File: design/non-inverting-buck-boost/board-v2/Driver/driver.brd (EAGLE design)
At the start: 5 parts

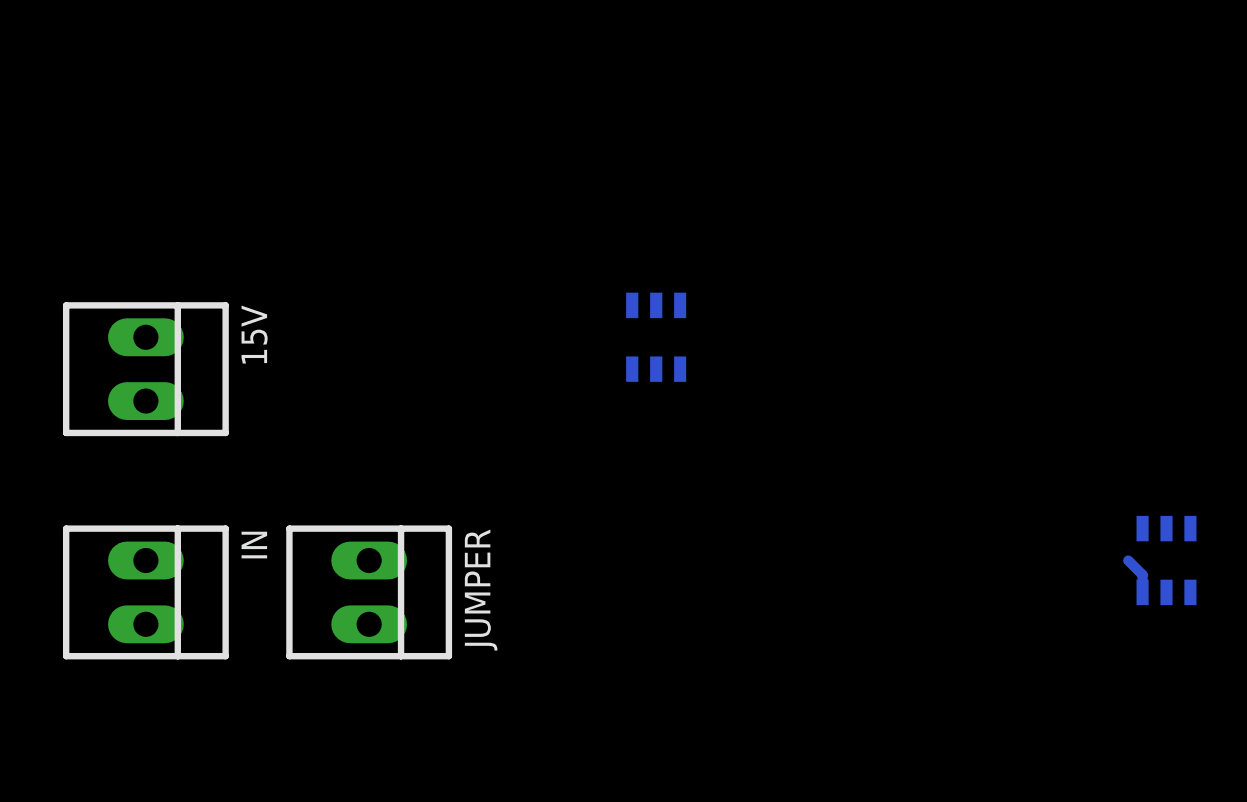
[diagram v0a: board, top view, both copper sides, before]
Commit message: finished driver board layout
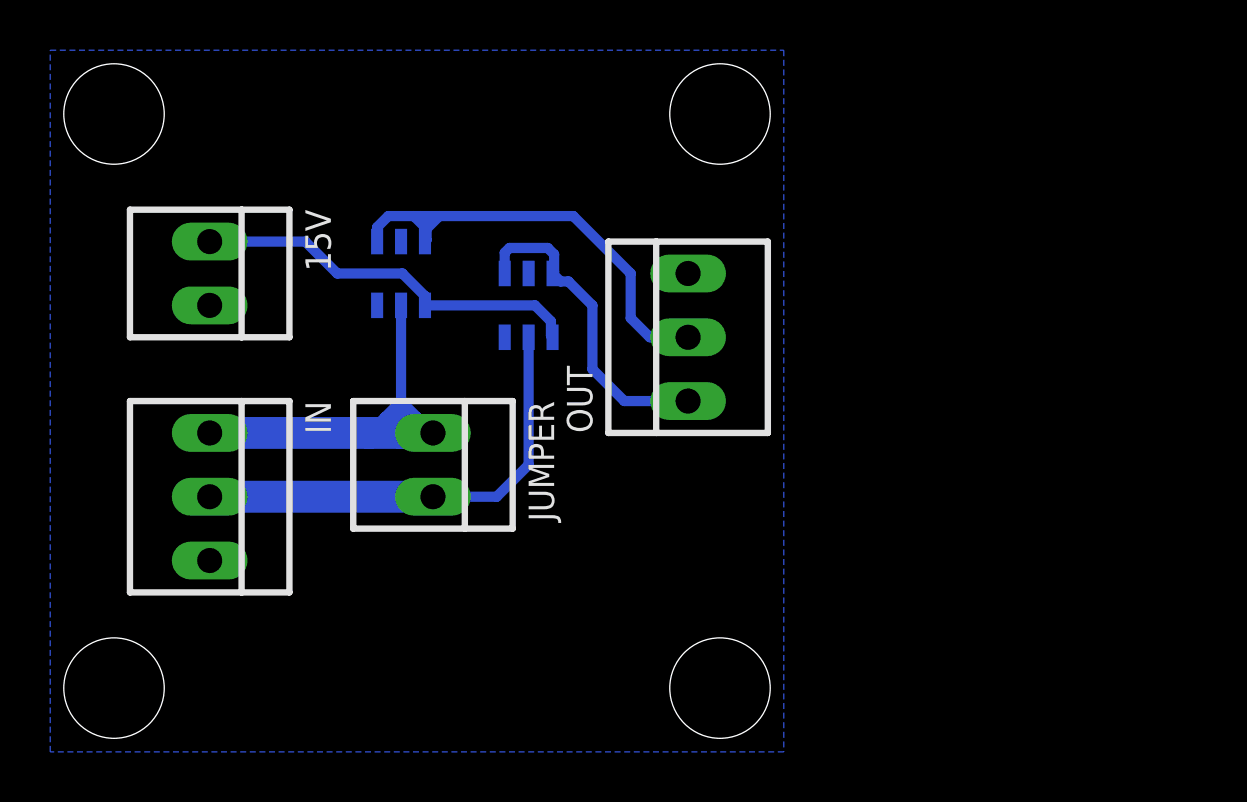
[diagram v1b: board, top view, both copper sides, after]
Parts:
- added OUT: 22-23-2031, con-molex:22-23-2031
- IN: value (none) -> 22-23-2031; device con-molex:22-23-2021 -> con-molex:22-23-2031
- moved IC2 32.6 mm to (15.2, 20.3)
- moved JUMPER 5.68 mm to (16.5, 12.7)
- moved IC1 5.24 mm to (20.3, 19.1)
- moved IN 4.58 mm to (7.62, 11.4)
- moved 15V 4.58 mm to (7.62, 20.3)
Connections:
- removed net 15V-: 15V.2, IC1.3, IC2.3
- new net GND: 15V.2, IC1.3, IC2.3, IN.3, OUT.3
- net IN1: now also IC2.2; no longer IC1.2
- net IN2: now also IC1.2; no longer IC2.2
- net N$5: now also OUT.1
- net N$6: now also OUT.2
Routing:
- net N$6: track 0.00 -> 19.8 mm
- net IN1: track 0.00 -> 18.8 mm
- net IN2: track 0.00 -> 18.3 mm
- net 15V+: track 0.00 -> 15.8 mm
- net N$5: track 0.00 -> 12.8 mm
- net 15V-: track 1.51 -> 0.00 mm
- added copper zone on layer 16, net GND
